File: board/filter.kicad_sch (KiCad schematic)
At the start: 79 parts, among them J10 CV2, J8 QCV, J9 CV1, Q1 BC858, Q3 BC858, U10 TL072, U5 TL074, U6 LM13700, U7 LM13700, U8 TL072, U9 TL072

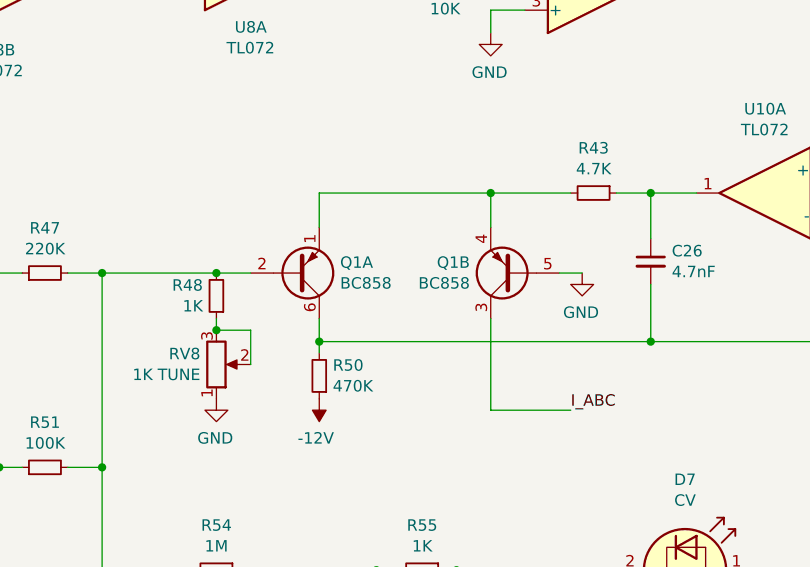
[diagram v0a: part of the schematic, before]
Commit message: Update panel and add jlcpcb assembly files
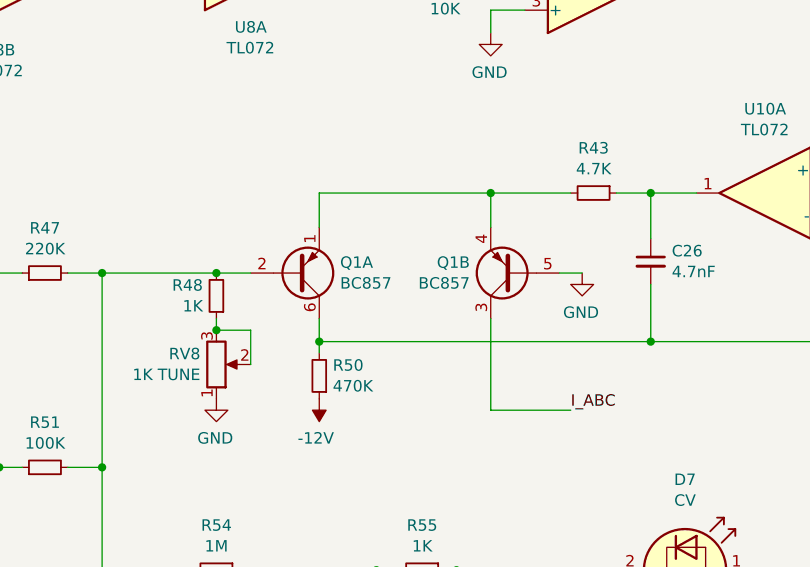
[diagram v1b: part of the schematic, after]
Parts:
- Q1: value BC858 -> BC857
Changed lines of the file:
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@@
       (effects (font (size 1.27 1.27)) (justify left))
     )
-    (property "Value" "BC858" (id 1) (at 122.1486 144.653 0)
+    (property "Value" "BC857" (id 1) (at 122.1486 144.653 0)
       (effects (font (size 1.27 1.27)) (justify left))
     )
@@
       (effects (font (size 1.27 1.27)) (justify left))
     )
-    (property "Value" "BC858" (id 1) (at 107.7214 144.653 0)
+    (property "Value" "BC857" (id 1) (at 107.7214 144.653 0)
       (effects (font (size 1.27 1.27)) (justify left))
     )

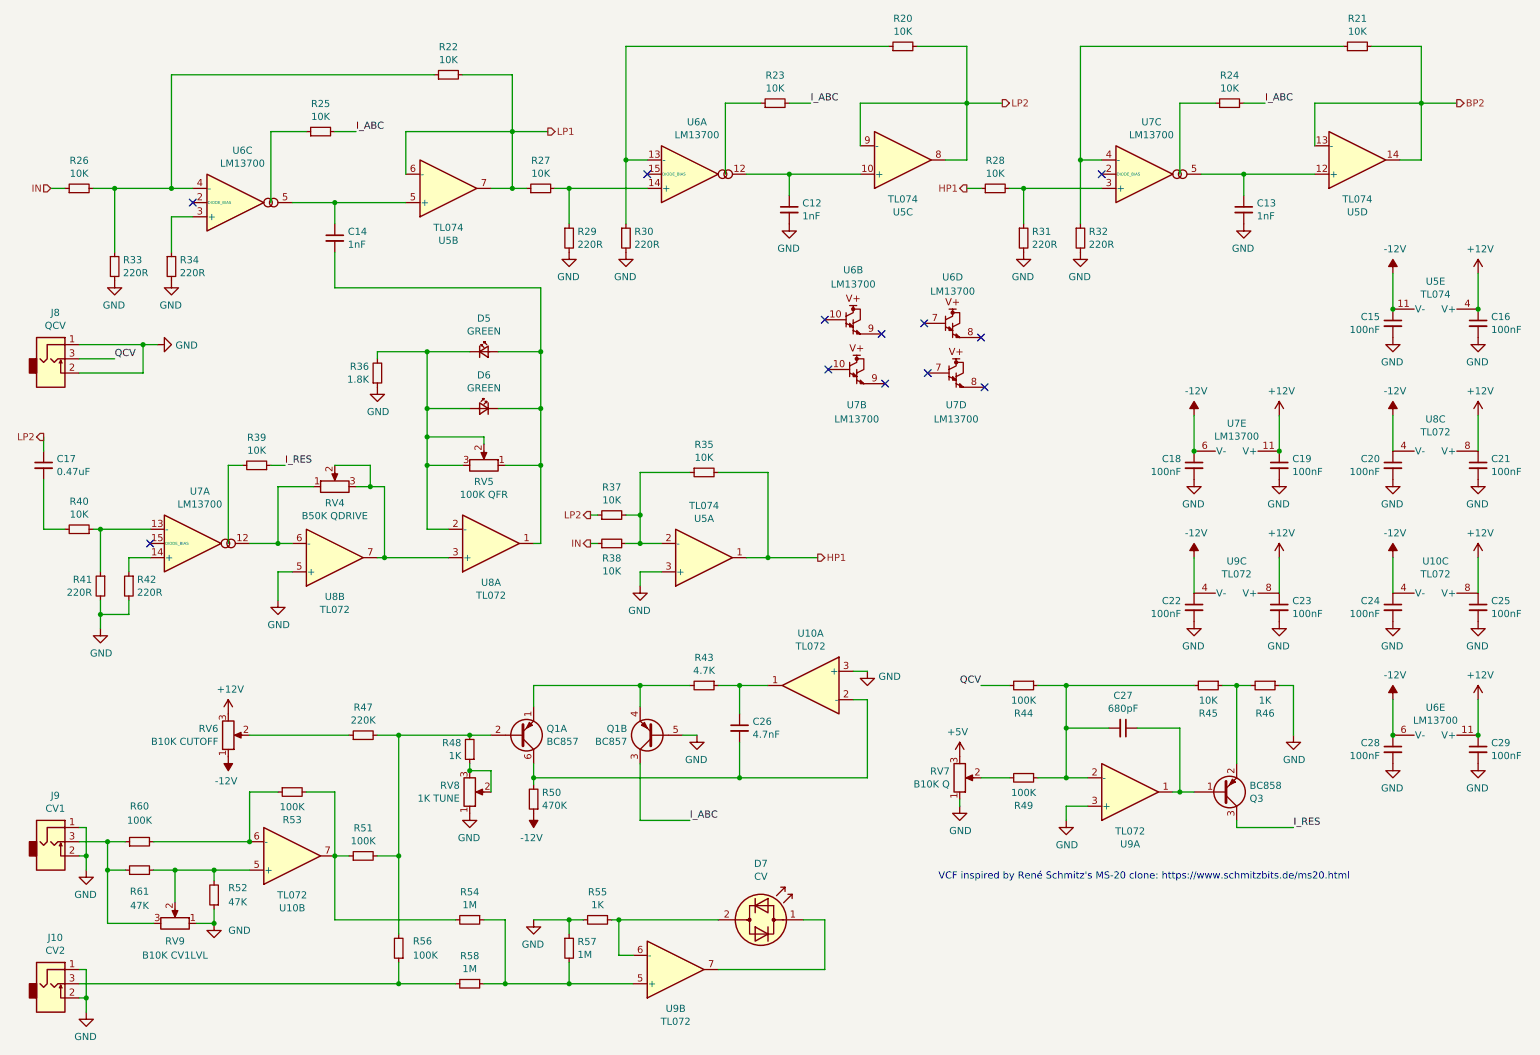
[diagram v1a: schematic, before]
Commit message: fix resonance gain and simplify module calibration
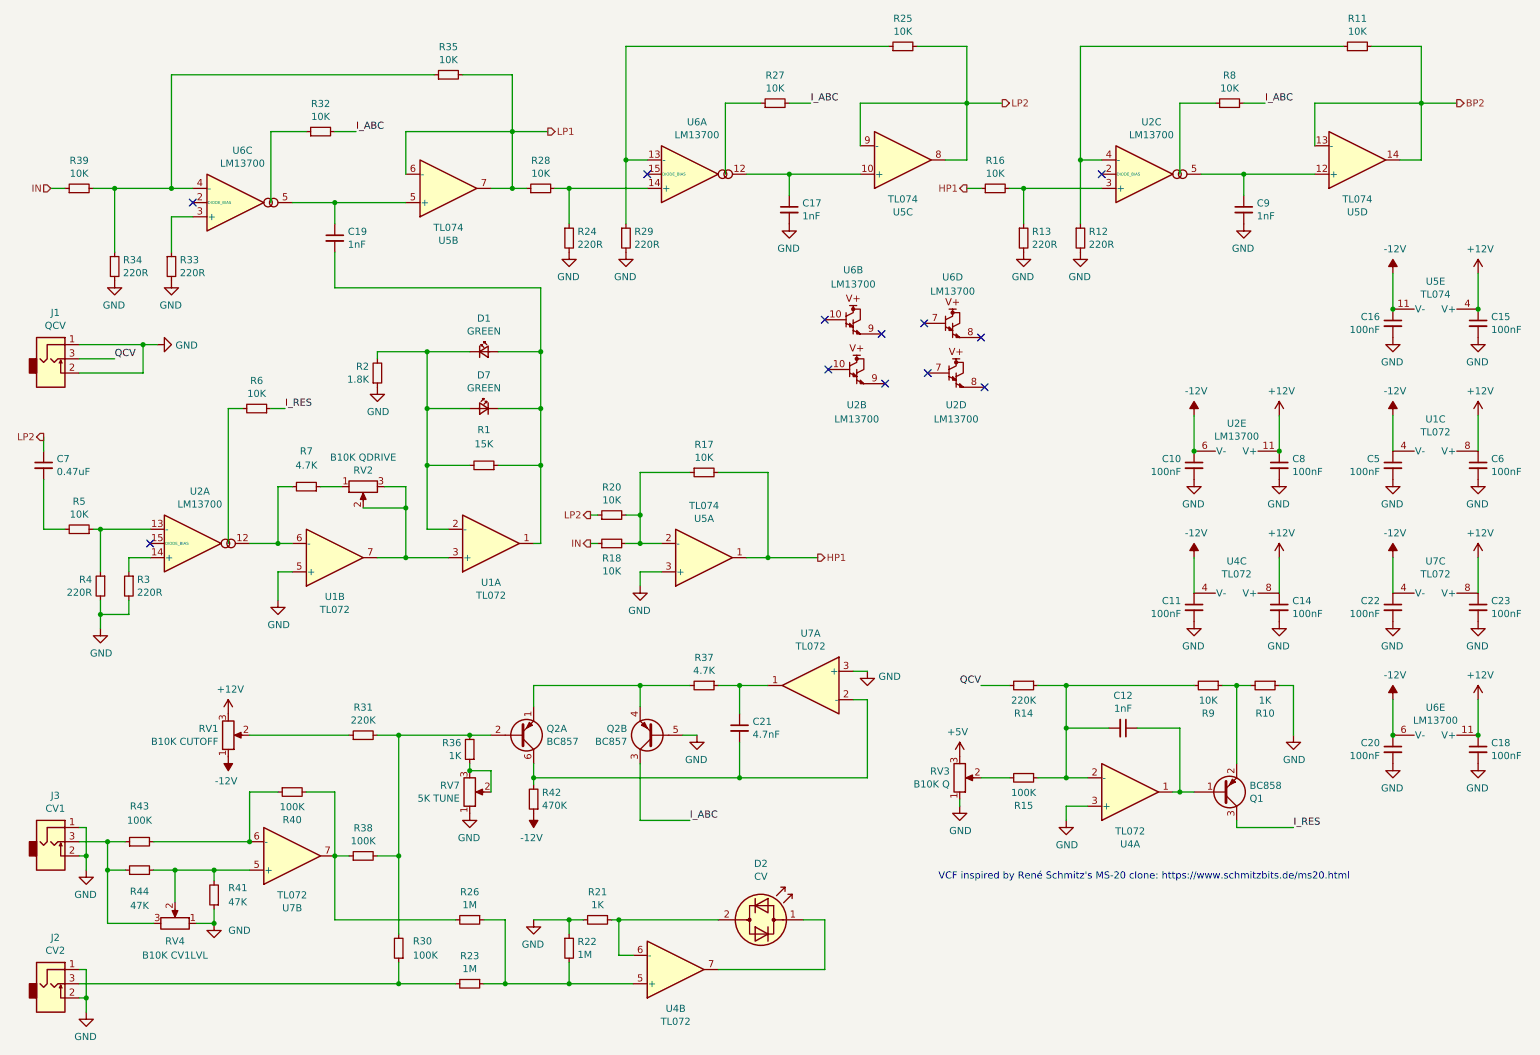
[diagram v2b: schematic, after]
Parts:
- removed RV5: 100K QFR, Potentiometer_SMD:Potentiometer_Bourns_TC33X_Vertical, symbol vcf-20-rescue:R_POT-Device
- added R1: 15K, Resistor_SMD:R_0603_1608Metric, symbol Device:R_Small
- added R7: 4.7K, Resistor_SMD:R_0603_1608Metric, symbol Device:R_Small
- C12: renamed from C27; value 680pF -> 1nF
- R14: renamed from R44; value 100K -> 220K
- RV2: renamed from RV4; value B50K QDRIVE -> B10K QDRIVE
- RV7: renamed from RV8; value 1K TUNE -> 5K TUNE
- renumbered C18 to C10, C22 to C11, C23 to C14, C16 to C15, C15 to C16, C12 to C17, C29 to C18, C14 to C19, C28 to C20, C26 to C21, C24 to C22, C25 to C23, C20 to C5, C21 to C6, C17 to C7, C19 to C8, C13 to C9, D5 to D1, D7 to D2, D6 to D7, J8 to J1, J10 to J2, J9 to J3, Q3 to Q1, Q1 to Q2, R46 to R10, R21 to R11, R32 to R12, R31 to R13, R49 to R15, R28 to R16, R35 to R17, R38 to R18, R36 to R2, R37 to R20, R55 to R21, R57 to R22, R58 to R23, R29 to R24, R20 to R25, R54 to R26, R23 to R27, R27 to R28, R30 to R29, R42 to R3, R56 to R30, R47 to R31, R25 to R32, R34 to R33, R33 to R34, R22 to R35, R48 to R36, R43 to R37, R51 to R38, R26 to R39, R41 to R4, R53 to R40, R52 to R41, R50 to R42, R60 to R43, R61 to R44, R40 to R5, R39 to R6, R24 to R8, R45 to R9, RV6 to RV1, RV7 to RV3, RV9 to RV4, U8 to U1, U7 to U2, U9 to U4, U10 to U7
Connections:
- net at C19.2, D1.2 (A), D7.1 (K)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: now also R1.1
- net at U1.6 (-), U2.12: now also R7.2; no longer RV2.1
- net at D1.1 (K), D7.2 (A), R2.2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: now also R1.2
- new net: R7.1, RV2.1
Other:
- moved on the sheet: R6, RV2

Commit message: fix back silkscreen and update production files
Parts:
- C10, C11, C14, C15, C16, C18, C20, C22, C23, C5, C6, C8: LCSC (none) -> C14663
- C12, C17, C19, C9: LCSC (none) -> C1588
- C21: LCSC (none) -> C338071
- C7: LCSC (none) -> C1623
- Q1: LCSC (none) -> C596216
- Q2: LCSC (none) -> C105887
- R1: LCSC (none) -> C22809
- R10, R21, R36: LCSC (none) -> C21190
- R11, R16, R17, R18, R20, R25, R27, R28, R32, R35, R39, R5, R6, R8, R9: LCSC (none) -> C25804
- R12, R13, R24, R29, R3, R33, R34, R4: LCSC (none) -> C22962
- R14, R31: LCSC (none) -> C22961
- R15, R30, R38, R40, R43: LCSC (none) -> C25803
- R2: LCSC (none) -> C4177
- R22, R23, R26: LCSC (none) -> C22935
- R37, R7: LCSC (none) -> C23162
- R41, R44: LCSC (none) -> C25819
- R42: LCSC (none) -> C23178
- RV7: LCSC (none) -> C719177
- U1, U4, U7: LCSC (none) -> C90748
- U2, U6: LCSC (none) -> C174050
- U5: LCSC (none) -> C96507
